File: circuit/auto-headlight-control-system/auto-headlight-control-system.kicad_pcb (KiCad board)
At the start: 2 copper layers, 142.2 x 88.9 mm, 16 parts, among them J1 Serial_Tx_1, J2 Serial_GND_1, J3 Serial_Tx_2, J4 Serial_GND_2, M1 SG90, T1 SN65HVD230, T2 SN65HVD230, U1 STM32_L, U2 STM32_R, U3 STM32_L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

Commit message: Compact: PCB
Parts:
- added  : Pin_D1.0mm_L10.0mm, Connector_Pin:Pin_D1.0mm_L10.0mm, F.Cu at (138.4, 38.1)
- added  : Pin_D1.0mm_L10.0mm, Connector_Pin:Pin_D1.0mm_L10.0mm, F.Cu at (166.4, 96.5)
- added  : Pin_D1.0mm_L10.0mm, Connector_Pin:Pin_D1.0mm_L10.0mm, F.Cu at (81.3, 111.8)
- added  : Pin_D1.0mm_L10.0mm, Connector_Pin:Pin_D1.0mm_L10.0mm, F.Cu at (53.3, 38.1)
- moved S1 28.5 mm to (55.9, 109.2), turned to 180 degrees
- moved M1 25.4 mm to (144.8, 96.5), turned to 180 degrees
- moved R1 17.7 mm to (138.4, 71.1)
- moved J2 16.1 mm to (57.1, 44.5)
- moved J4 14.8 mm to (144.8, 44.5)
- moved U4 11.4 mm to (166.4, 39.4)
- moved T1 11.4 mm to (57.1, 72.4)
- moved U2 8.89 mm to (78.7, 39.4)
- moved D2 6.35 mm to (138.4, 64.8)
- moved T2 6.35 mm to (144.8, 72.4)
- moved S2 5.39 mm to (74.9, 102.9)
- moved J1 5.08 mm to (57.1, 52.1)
- moved D1 3.81 mm to (144.8, 64.8)
- moved J3 3.81 mm to (144.8, 52.1)
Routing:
- net 3V3_1: track 70.4 -> 57.0 mm
- net PWM: track 39.7 -> 51.4 mm
- net CAN_TX_1: track 17.8 -> 6.35 mm
- net CAN_RX_1: track 17.8 -> 6.35 mm
- net 5V: track 25.3 -> 16.3 mm
- net SDA: track 51.3 -> 43.3 mm
- net CAN_TX_2: track 12.7 -> 6.35 mm
- net CAN_RX_2: track 12.7 -> 6.35 mm
- net Serial_Tx_1: track 11.4 -> 6.35 mm
- net 3V3_2: track 24.2 -> 20.1 mm
- net Serial_Tx_2: track 10.2 -> 6.35 mm
- net Net-(D2-Pad1): track 10.2 -> 6.35 mm
- net Net-(D1-Pad1): track 10.2 -> 6.35 mm
- net SCL: track 54.9 -> 51.9 mm
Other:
- board size 142.2 x 88.9 mm -> 119.4 x 80 mm
- board text added: "Actuator kmkim"
- board text added: "Sensor kmkim"
- board text removed: "Actuator by kmkim"
- board text removed: "Sensor by kmkim"

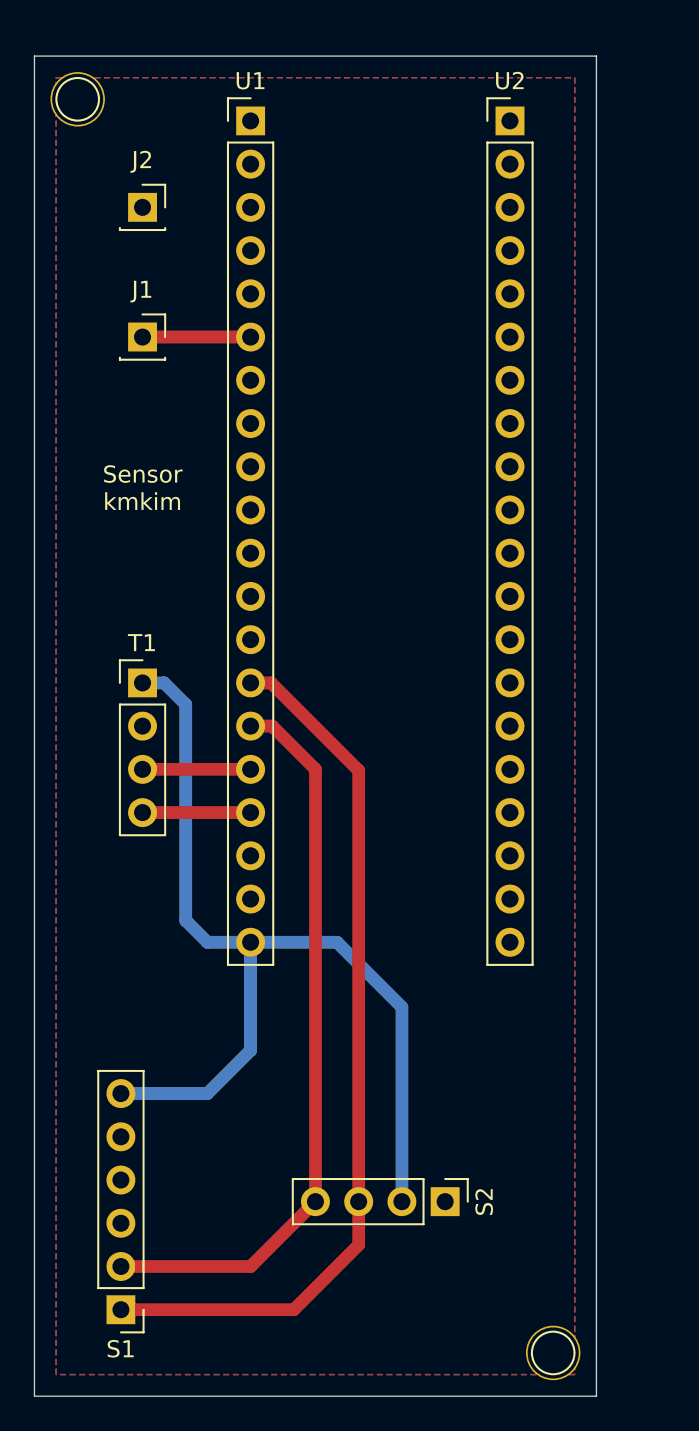
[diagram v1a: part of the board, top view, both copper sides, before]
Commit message: Fix: PCB size
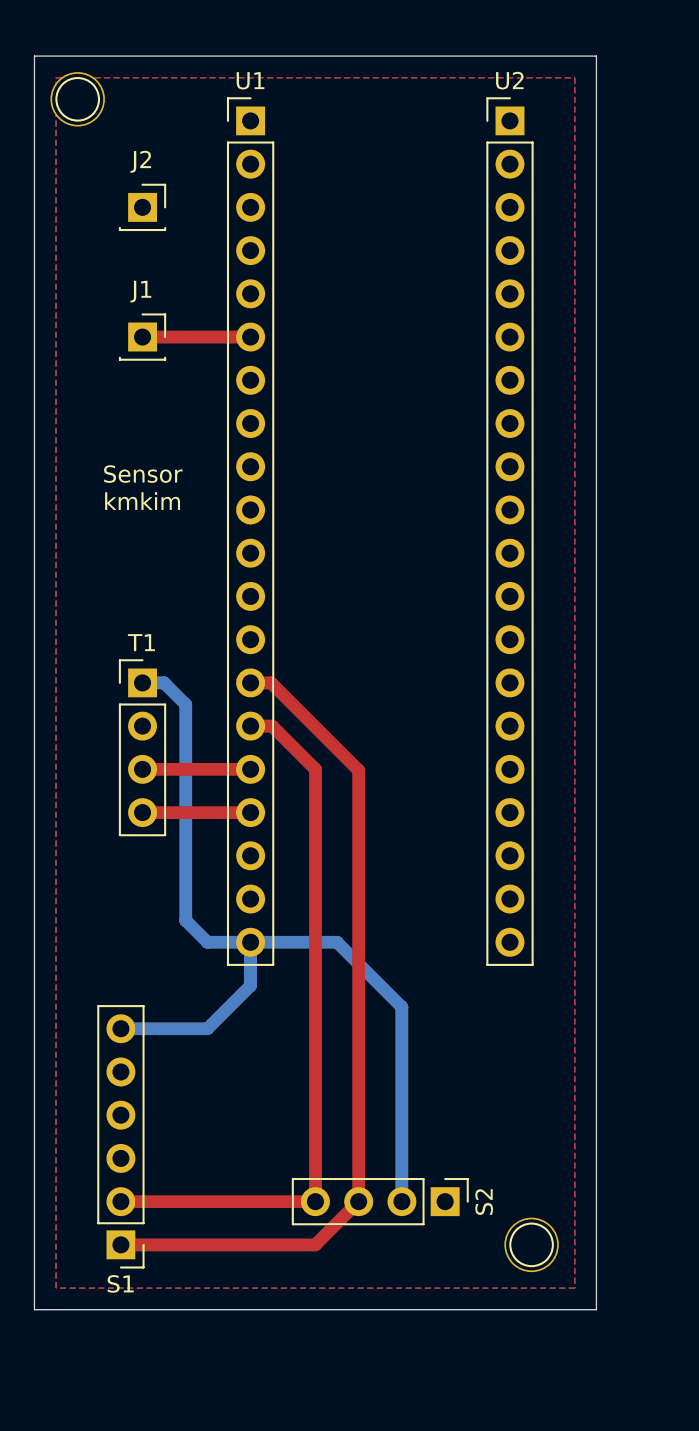
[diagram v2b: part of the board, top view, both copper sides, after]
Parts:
- moved   6.48 mm to (80.0, 105.4)
- moved S1 3.81 mm to (55.9, 105.4)
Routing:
- net 3V3_1: track 57.0 -> 53.2 mm
- net SCL: track 51.9 -> 48.8 mm
- net SDA: track 43.3 -> 41.7 mm
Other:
- board size 119.4 x 80 mm -> 119.4 x 74.9 mm

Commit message: Update: merge PCB
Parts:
- moved   47.0 mm to (119.4, 97.8)
- moved   47.0 mm to (91.4, 39.4)
- moved D2 47.0 mm to (91.4, 66.0)
- moved R1 47.0 mm to (91.4, 72.4)
- moved U4 47.0 mm to (119.4, 40.6)
- moved D1 47.0 mm to (97.8, 66.0)
- moved J3 47.0 mm to (97.8, 53.3)
- moved J4 47.0 mm to (97.8, 45.7)
- moved M1 47.0 mm to (97.8, 97.8)
- moved T2 47.0 mm to (97.8, 73.7)
- moved U3 47.0 mm to (104.1, 40.6)
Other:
- board size 119.4 x 74.9 mm -> 72.4 x 73.7 mm
